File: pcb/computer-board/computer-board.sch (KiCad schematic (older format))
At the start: 26 parts, among them J1 Conn_01x02_Male, J2 Conn_01x02_Male, J3 Conn_02x03_Counter_Clockwise, SW1 SW_Push, U1 TLV73333PDBV, U2 YC248, U3 YC248

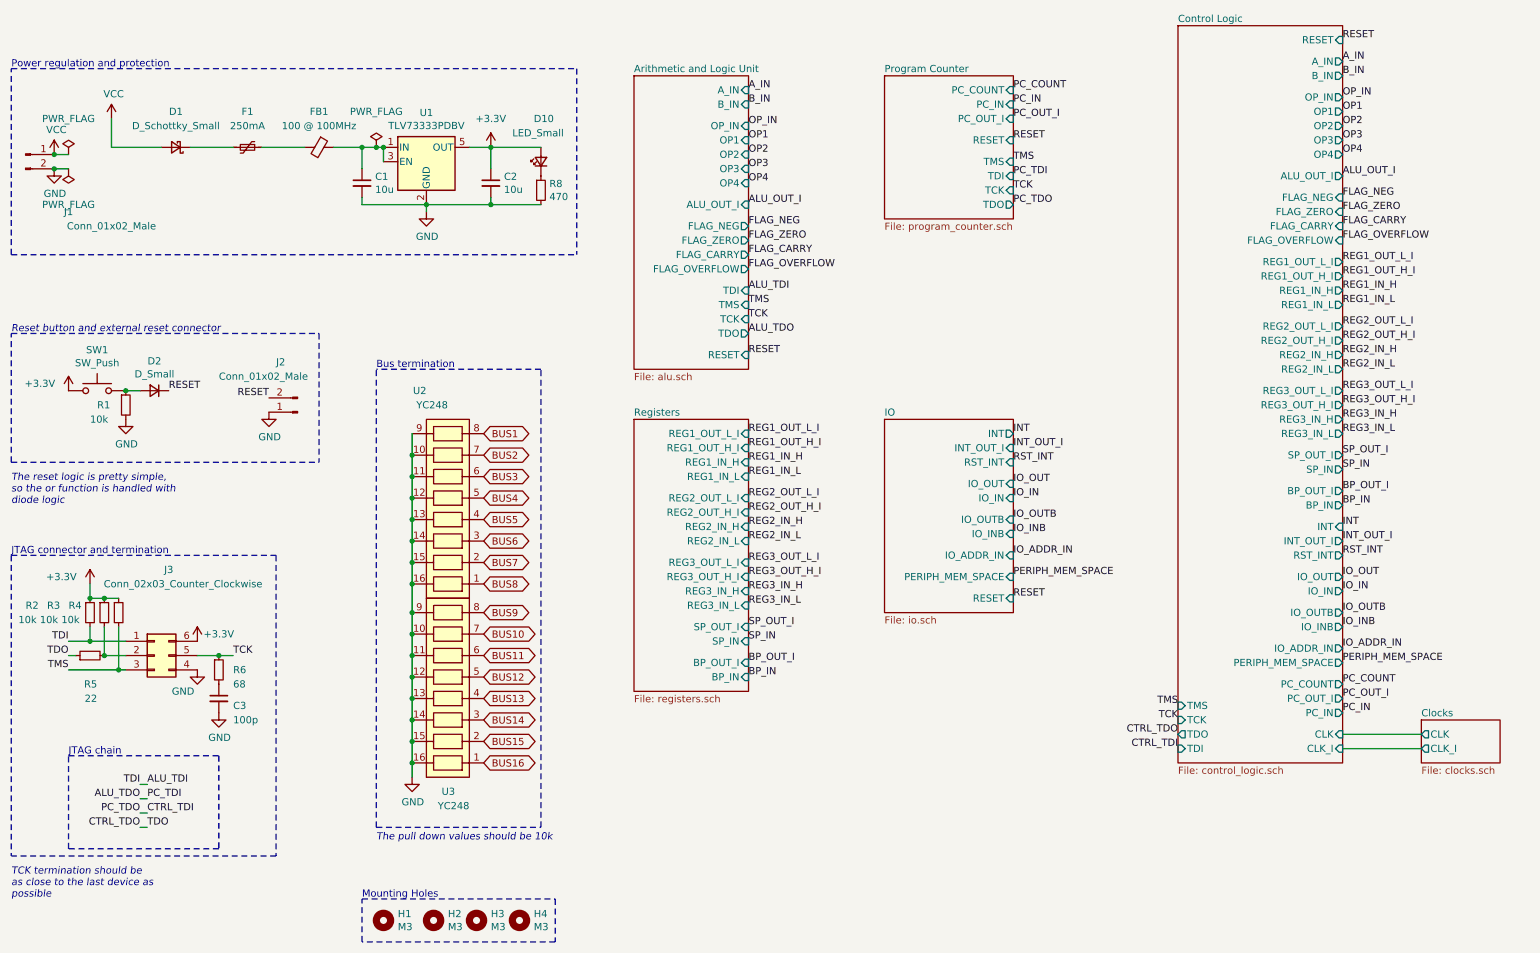
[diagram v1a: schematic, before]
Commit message: Remove and change connectors for a mezzanine one
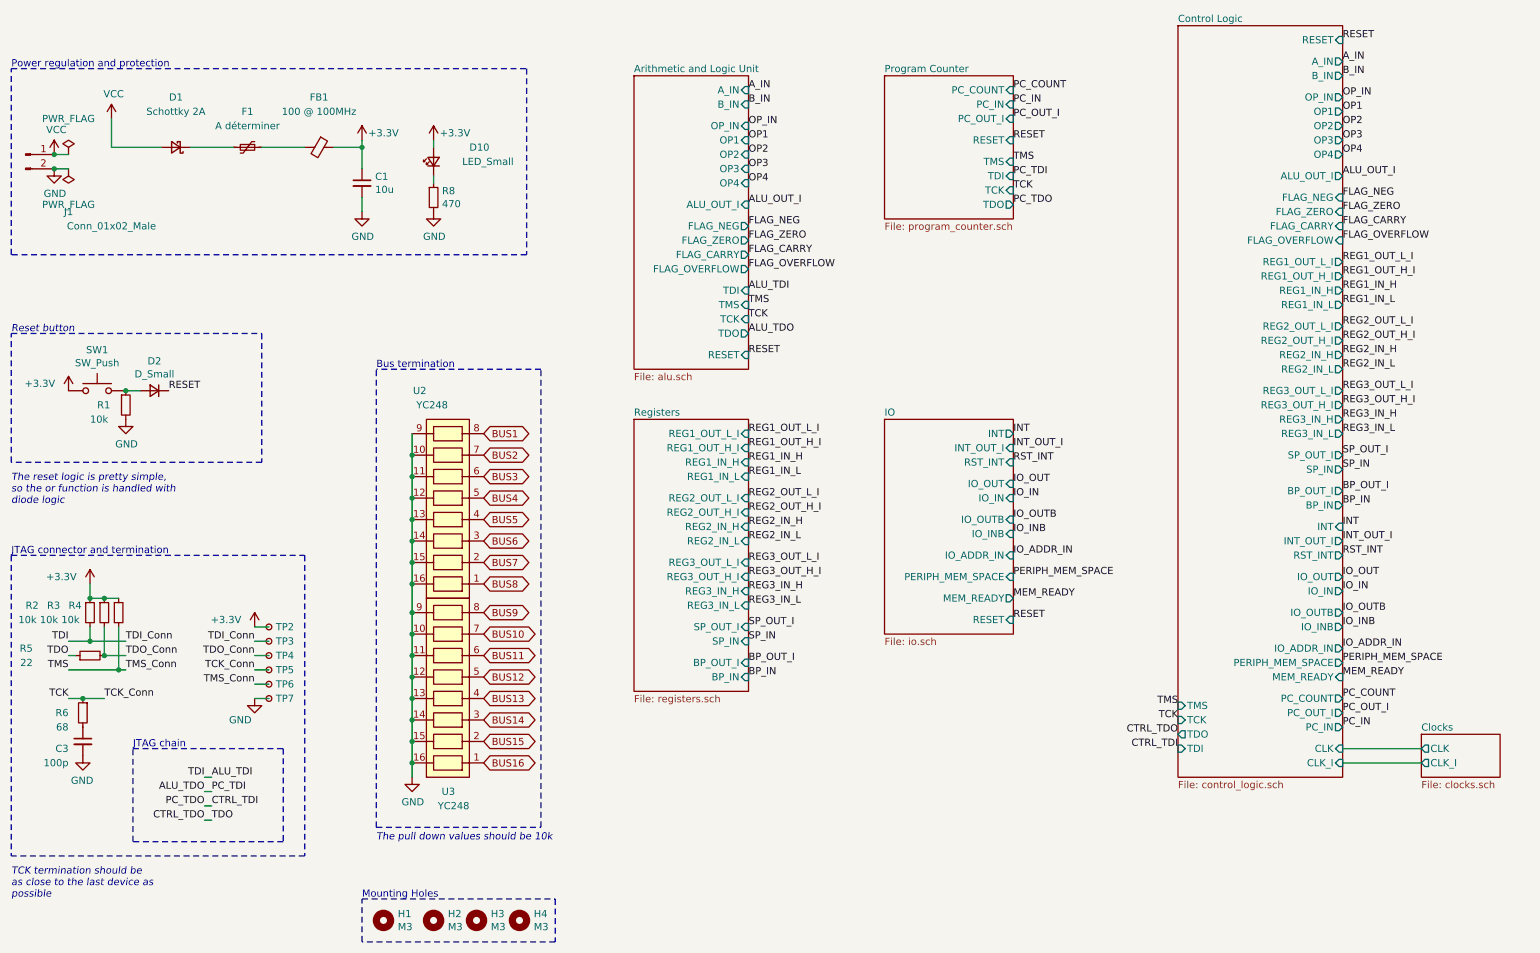
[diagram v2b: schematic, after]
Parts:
- removed C2: 10u, Capacitor_SMD:C_0603_1608Metric, symbol Device:C_Small
- removed J2: Conn_01x02_Male, Connector_Molex:Molex_Pico-Clasp_202396-0207_1x02-1MP_P1.00mm_Horizontal, symbol Connector:Conn_01x02_Male
- removed J3: Conn_02x03_Counter_Clockwise, Connector_Molex:Molex_Pico-Clasp_202396-0607_1x06-1MP_P1.00mm_Horizontal, symbol Connector_Generic:Conn_02x03_Counter_Clockwise
- removed U1: TLV73333PDBV, Package_TO_SOT_SMD:SOT-23-5, symbol Regulator_Linear:TLV73333PDBV
- added TP2, TP3, TP4, TP5, TP6, TP7: TestPoint_Small, TestPoint:TestPoint_THTPad_D1.5mm_Drill0.7mm, symbol Connector:TestPoint_Small
- C1: footprint Capacitor_SMD:C_0603_1608Metric -> Capacitor_SMD:C_0603_1608Metric_Pad1.08x0.95mm_HandSolder
- D1: value D_Schottky_Small -> Schottky 2A; footprint Diode_SMD:D_0603_1608Metric_Pad1.05x0.95mm_HandSolder -> Diode_SMD:D_SOD-123
- F1: value 250mA -> A déterminer; footprint Fuse:Fuse_1206_3216Metric_Pad1.42x1.75mm_HandSolder -> Fuse:Fuse_1210_3225Metric_Pad1.42x2.65mm_HandSolder
- FB1: footprint Resistor_SMD:R_0603_1608Metric -> Inductor_SMD:L_0805_2012Metric_Pad1.15x1.40mm_HandSolder
- J1: footprint Connector_Molex:Molex_Pico-Clasp_202396-0207_1x02-1MP_P1.00mm_Horizontal -> Connector_JST:JST_PH_S2B-PH-K_1x02_P2.00mm_Horizontal
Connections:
- net +3V3: now also C1.1, FB1.1, TP2.1
- net ALU_TDI: now also TP3.1
- net GND: now also TP7.1
- net TCK: now also TP5.1
- net TMS: now also TP6.1
- net TDO_Conn: now reaches R3.2, R5.2
- net TDO_Conn: now also TP4.1
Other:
- note added: "Reset button"
- note removed: "Reset button and external reset connector"
- moved on the sheet: C3, D10, R6, R8

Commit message: Revision 2 is ready
Need to wait for the testing of rev 1 before ordering
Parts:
- TP2, TP3, TP4, TP5, TP6, TP7: footprint TestPoint:TestPoint_THTPad_D1.5mm_Drill0.7mm -> TestPoint:TestPoint_THTPad_1.5x1.5mm_Drill0.7mm
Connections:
- net GND: now also J1.1 (Pin_1); no longer J1.2 (Pin_2)
- net VCC: now also J1.2 (Pin_2); no longer J1.1 (Pin_1)
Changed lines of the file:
@@
 F49 "MEM_READY" I R 10150 5500 50
 $EndSheet
-Wire Wire Line
-	10700 6100 10150 6100
-Wire Wire Line
-	10150 6000 10700 6000
 $Sheet
-S 10700 5900 550  300
+S 5200 6400 550  400
 U 5F97DC64
 F0 "Clocks" 50
 F1 "clocks.sch" 50
-F2 "CLK" O L 10700 6000 50
-F3 "CLK_I" O L 10700 6100 50
+F2 "CLK" O R 5750 6600 50
+F3 "CLK_I" O R 5750 6500 50
+F4 "EXT_CLK" I R 5750 6700 50
 $EndSheet
 $Comp
@@
 CTRL_TDO
 $Sheet
-S 6950 3700 900  1500
+S 6950 3700 900  1850
 U 5F8B5DB4
 F0 "IO" 50
@@
 F9 "IO_INB" I R 7850 4500 50
 F10 "IO_ADDR_IN" I R 7850 4650 50
-F11 "RESET" I R 7850 5100 50
+F11 "RESET" I R 7850 5450 50
 F12 "MEM_READY" O R 7850 4950 50
+F13 "CLK" I R 7850 5100 50
+F14 "EXT_CLK" O R 7850 5300 50
+F15 "CLK_I" I R 7850 5200 50
 $EndSheet
 $Sheet
@@
 Text Label 7850 4800 0    50   ~ 0
 PERIPH_MEM_SPACE
-Text Label 7850 5100 0    50   ~ 0
+Text Label 7850 5450 0    50   ~ 0
 RESET
 Text Label 10150 1200 0    50   ~ 0
@@
 L Connector:Conn_01x02_Male J1
 U 1 1 5FAF8387
-P 950 1850
-F 0 "J1" H 1250 1450 50  0000 C CNN
-F 1 "Conn_01x02_Male" H 1550 1350 50  0000 C CNN
-F 2 "Connector_JST:JST_PH_S2B-PH-K_1x02_P2.00mm_Horizontal" H 950 1850 50  0001 C CNN
-F 3 "~" H 950 1850 50  0001 C CNN
-	1    950  1850
-	1    0    0    -1
+P 950 1950
+F 0 "J1" H 1250 1550 50  0000 C CNN
+F 1 "Conn_01x02_Male" H 1550 1450 50  0000 C CNN
+F 2 "Connector_JST:JST_PH_S2B-PH-K_1x02_P2.00mm_Horizontal" H 950 1950 50  0001 C CNN
+F 3 "~" H 950 1950 50  0001 C CNN
+	1    950  1950
+	1    0    0    1
 $EndComp
 $Comp
@@
 Wire Wire Line
 	1150 1850 1250 1850
-Connection ~ 1150 1850
 $Comp
 L power:PWR_FLAG #FLG0103
@@
 Wire Wire Line
 	1150 1950 1250 1950
-Connection ~ 1150 1950
 Wire Wire Line
 	2200 6500 2250 6500
@@
 F 0 "TP2" H 2698 5150 50  0000 L CNN
 F 1 "TestPoint_Small" H 2698 5105 50  0001 L CNN
-F 2 "TestPoint:TestPoint_THTPad_D1.5mm_Drill0.7mm" H 2850 5150 50  0001 C CNN
+F 2 "TestPoint:TestPoint_THTPad_1.5x1.5mm_Drill0.7mm" H 2850 5150 50  0001 C CNN
 F 3 "~" H 2850 5150 50  0001 C CNN
 	1    2650 5150
@@
 F 0 "TP3" H 2698 5250 50  0000 L CNN
 F 1 "TestPoint_Small" H 2698 5205 50  0001 L CNN
-F 2 "TestPoint:TestPoint_THTPad_D1.5mm_Drill0.7mm" H 2850 5250 50  0001 C CNN
+F 2 "TestPoint:TestPoint_THTPad_1.5x1.5mm_Drill0.7mm" H 2850 5250 50  0001 C CNN
 F 3 "~" H 2850 5250 50  0001 C CNN
 	1    2650 5250
@@
 F 0 "TP4" H 2698 5350 50  0000 L CNN
 F 1 "TestPoint_Small" H 2698 5305 50  0001 L CNN
-F 2 "TestPoint:TestPoint_THTPad_D1.5mm_Drill0.7mm" H 2850 5350 50  0001 C CNN
+F 2 "TestPoint:TestPoint_THTPad_1.5x1.5mm_Drill0.7mm" H 2850 5350 50  0001 C CNN
 F 3 "~" H 2850 5350 50  0001 C CNN
 	1    2650 5350
@@
 F 0 "TP5" H 2698 5450 50  0000 L CNN
 F 1 "TestPoint_Small" H 2698 5405 50  0001 L CNN
-F 2 "TestPoint:TestPoint_THTPad_D1.5mm_Drill0.7mm" H 2850 5450 50  0001 C CNN
+F 2 "TestPoint:TestPoint_THTPad_1.5x1.5mm_Drill0.7mm" H 2850 5450 50  0001 C CNN
 F 3 "~" H 2850 5450 50  0001 C CNN
 	1    2650 5450
@@
 F 0 "TP6" H 2698 5550 50  0000 L CNN
 F 1 "TestPoint_Small" H 2698 5505 50  0001 L CNN
-F 2 "TestPoint:TestPoint_THTPad_D1.5mm_Drill0.7mm" H 2850 5550 50  0001 C CNN
+F 2 "TestPoint:TestPoint_THTPad_1.5x1.5mm_Drill0.7mm" H 2850 5550 50  0001 C CNN
 F 3 "~" H 2850 5550 50  0001 C CNN
 	1    2650 5550
@@
 F 0 "TP7" H 2698 5650 50  0000 L CNN
 F 1 "TestPoint_Small" H 2698 5605 50  0001 L CNN
-F 2 "TestPoint:TestPoint_THTPad_D1.5mm_Drill0.7mm" H 2850 5650 50  0001 C CNN
+F 2 "TestPoint:TestPoint_THTPad_1.5x1.5mm_Drill0.7mm" H 2850 5650 50  0001 C CNN
 F 3 "~" H 2850 5650 50  0001 C CNN
 	1    2650 5650
@@
 Wire Wire Line
 	2550 5650 2650 5650
+Connection ~ 1150 1850
+Connection ~ 1150 1950
+Text Label 5750 6600 0    50   ~ 0
+CLK
+Text Label 5750 6500 0    50   ~ 0
+CLK_I
+Text Label 7850 5200 0    50   ~ 0
+CLK_I
+Text Label 7850 5100 0    50   ~ 0
+CLK
+Text Label 7850 5300 0    50   ~ 0
+EXT_CLK
+Text Label 5750 6700 0    50   ~ 0
+EXT_CLK
+Text Label 10150 6100 0    50   ~ 0
+CLK_I
+Text Label 10150 6000 0    50   ~ 0
+CLK
 $EndSCHEMATC

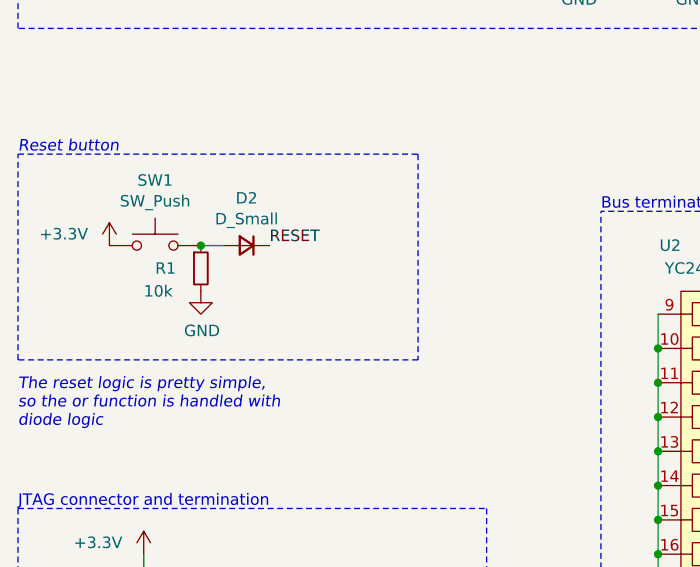
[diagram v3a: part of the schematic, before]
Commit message: added pulldowns on diode logic
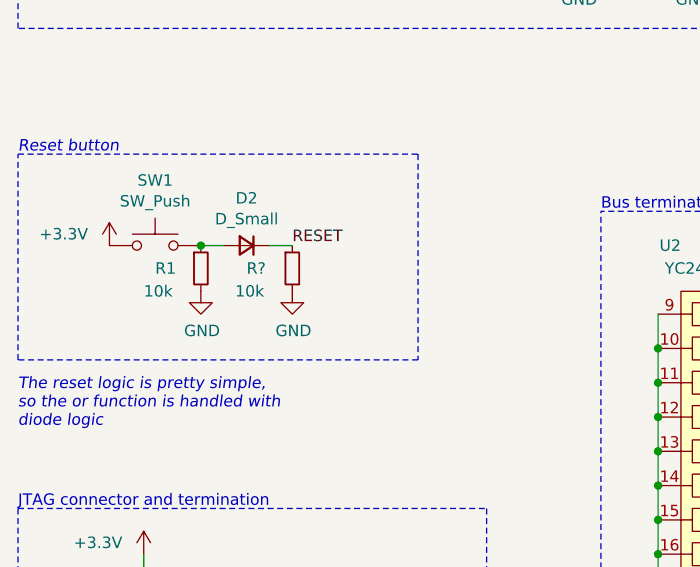
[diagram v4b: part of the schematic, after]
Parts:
- added R?: 10k, Resistor_SMD:R_0402_1005Metric_Pad0.72x0.64mm_HandSolder, symbol Device:R_Small
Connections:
- net GND: now also R?.2
- net RESET: now also R?.1
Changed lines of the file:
@@
 Wire Wire Line
 	1300 5350 1250 5350
-Text Label 1950 3500 0    50   ~ 0
+Text Label 2050 3500 0    50   ~ 0
 RESET
 Text Label 1250 5250 2    50   ~ 0
@@
 Text Label 10150 6000 0    50   ~ 0
 CLK
+$Comp
+L Device:R_Small R?
+U 1 1 60017274
+P 2050 3600
+F 0 "R?" H 1850 3600 50  0000 L CNN
+F 1 "10k" H 1800 3500 50  0000 L CNN
+F 2 "Resistor_SMD:R_0402_1005Metric_Pad0.72x0.64mm_HandSolder" H 2050 3600 50  0001 C CNN
+F 3 "~" H 2050 3600 50  0001 C CNN
+	1    2050 3600
+	1    0    0    -1
+$EndComp
+Wire Wire Line
+	1950 3500 2050 3500
+$Comp
+L power:GND #PWR?
+U 1 1 60018B39
+P 2050 3700
+AR Path="/5F97DCB2/60018B39" Ref="#PWR?"  Part="1"
+AR Path="/60018B39" Ref="#PWR?"  Part="1"
+F 0 "#PWR?" H 2050 3450 50  0001 C CNN
+F 1 "GND" H 2055 3527 50  0000 C CNN
+F 2 "" H 2050 3700 50  0001 C CNN
+F 3 "" H 2050 3700 50  0001 C CNN
+	1    2050 3700
+	1    0    0    -1
+$EndComp
 $EndSCHEMATC

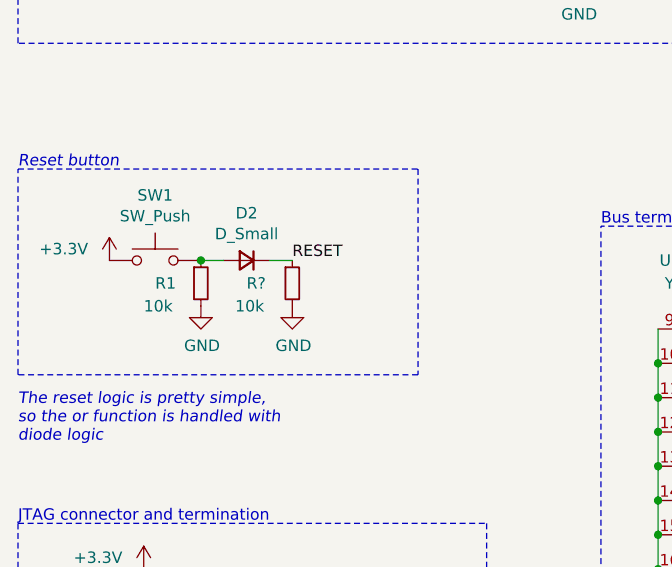
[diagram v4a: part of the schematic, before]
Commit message: added pulldowns on diode logic
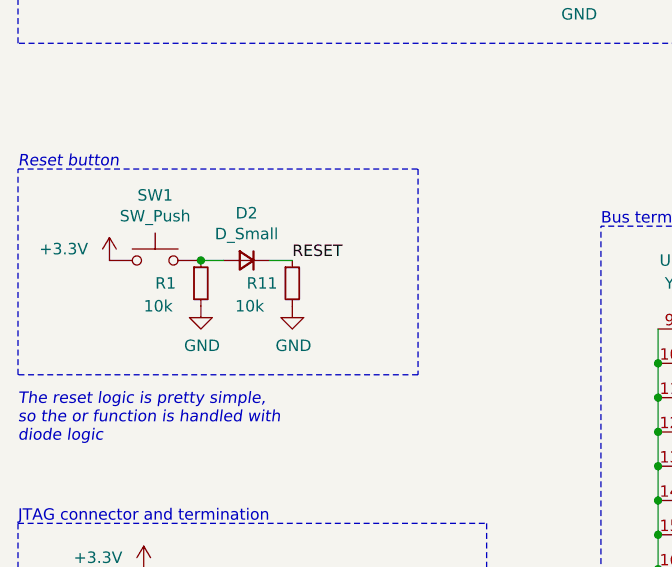
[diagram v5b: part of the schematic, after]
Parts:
- gave numbers to parts that had none: 1
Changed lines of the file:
@@
 CLK
 $Comp
-L Device:R_Small R?
+L Device:R_Small R11
 U 1 1 60017274
 P 2050 3600
-F 0 "R?" H 1850 3600 50  0000 L CNN
+F 0 "R11" H 1850 3600 50  0000 L CNN
 F 1 "10k" H 1800 3500 50  0000 L CNN
 F 2 "Resistor_SMD:R_0402_1005Metric_Pad0.72x0.64mm_HandSolder" H 2050 3600 50  0001 C CNN
@@
 P 2050 3700
 AR Path="/5F97DCB2/60018B39" Ref="#PWR?"  Part="1"
-AR Path="/60018B39" Ref="#PWR?"  Part="1"
-F 0 "#PWR?" H 2050 3450 50  0001 C CNN
+AR Path="/60018B39" Ref="#PWR0170"  Part="1"
+F 0 "#PWR0170" H 2050 3450 50  0001 C CNN
 F 1 "GND" H 2055 3527 50  0000 C CNN
 F 2 "" H 2050 3700 50  0001 C CNN
